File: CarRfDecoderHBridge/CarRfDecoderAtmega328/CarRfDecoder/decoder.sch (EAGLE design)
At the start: 55 parts, among them U2 RFM69CW, U3 MCP73831, U4 ATMEGA328P, U6 MIC5219 3.3V, Y1 16MHZ

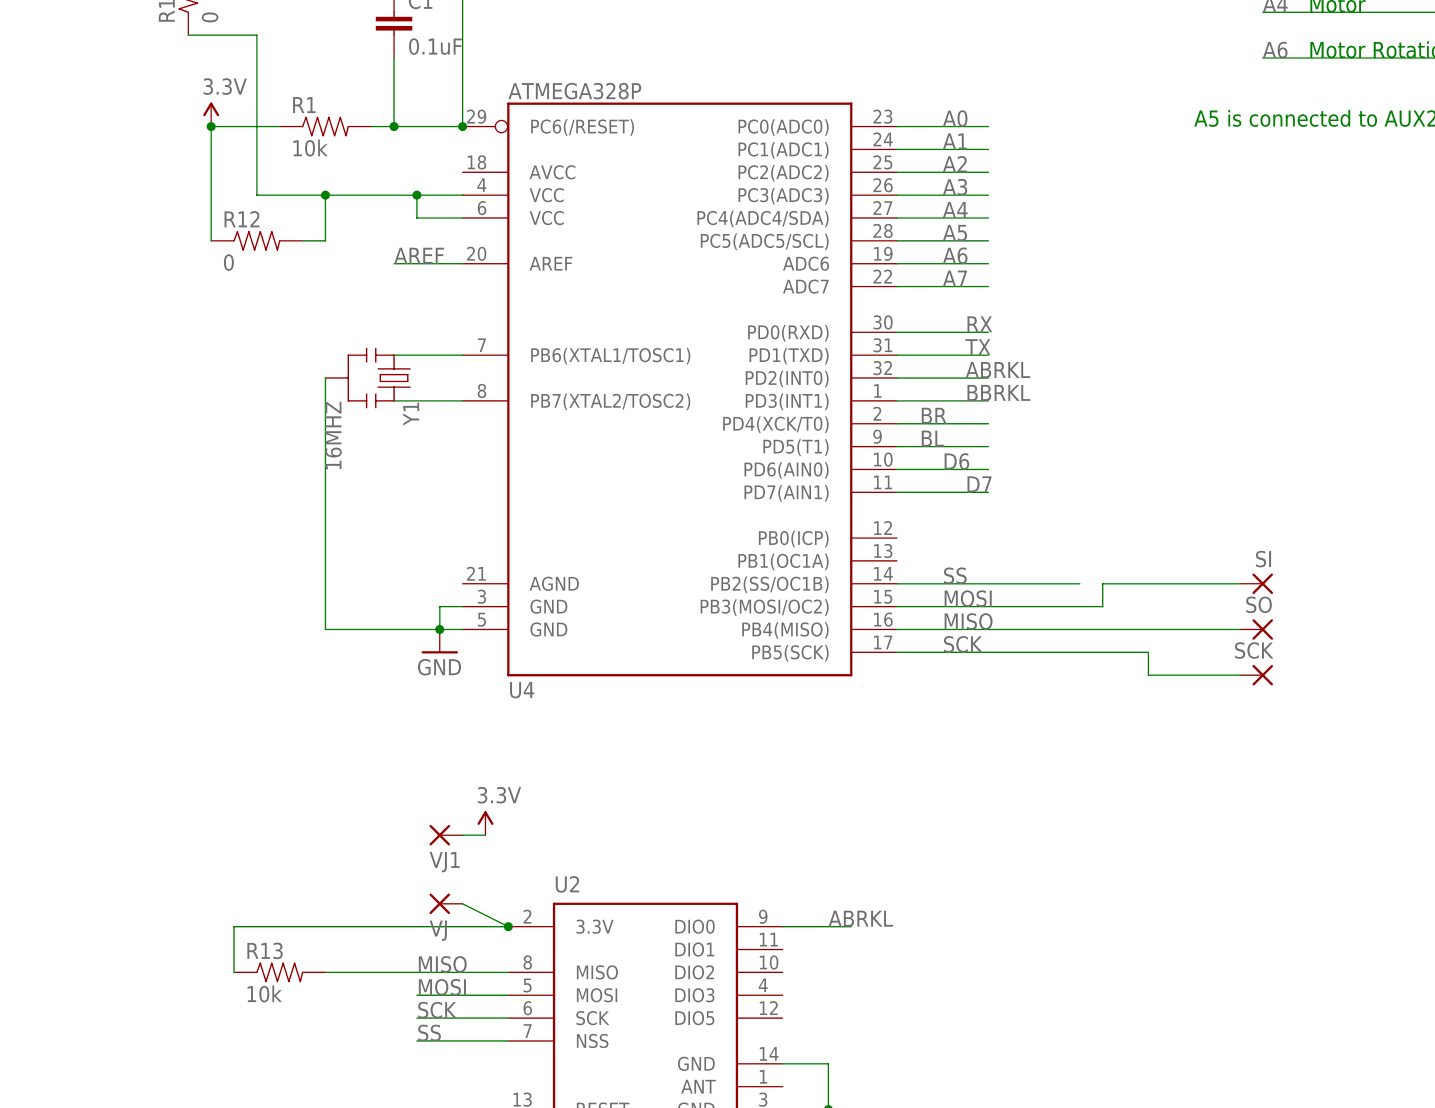
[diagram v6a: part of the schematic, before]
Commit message: Add a new version of the rc board, now smaller
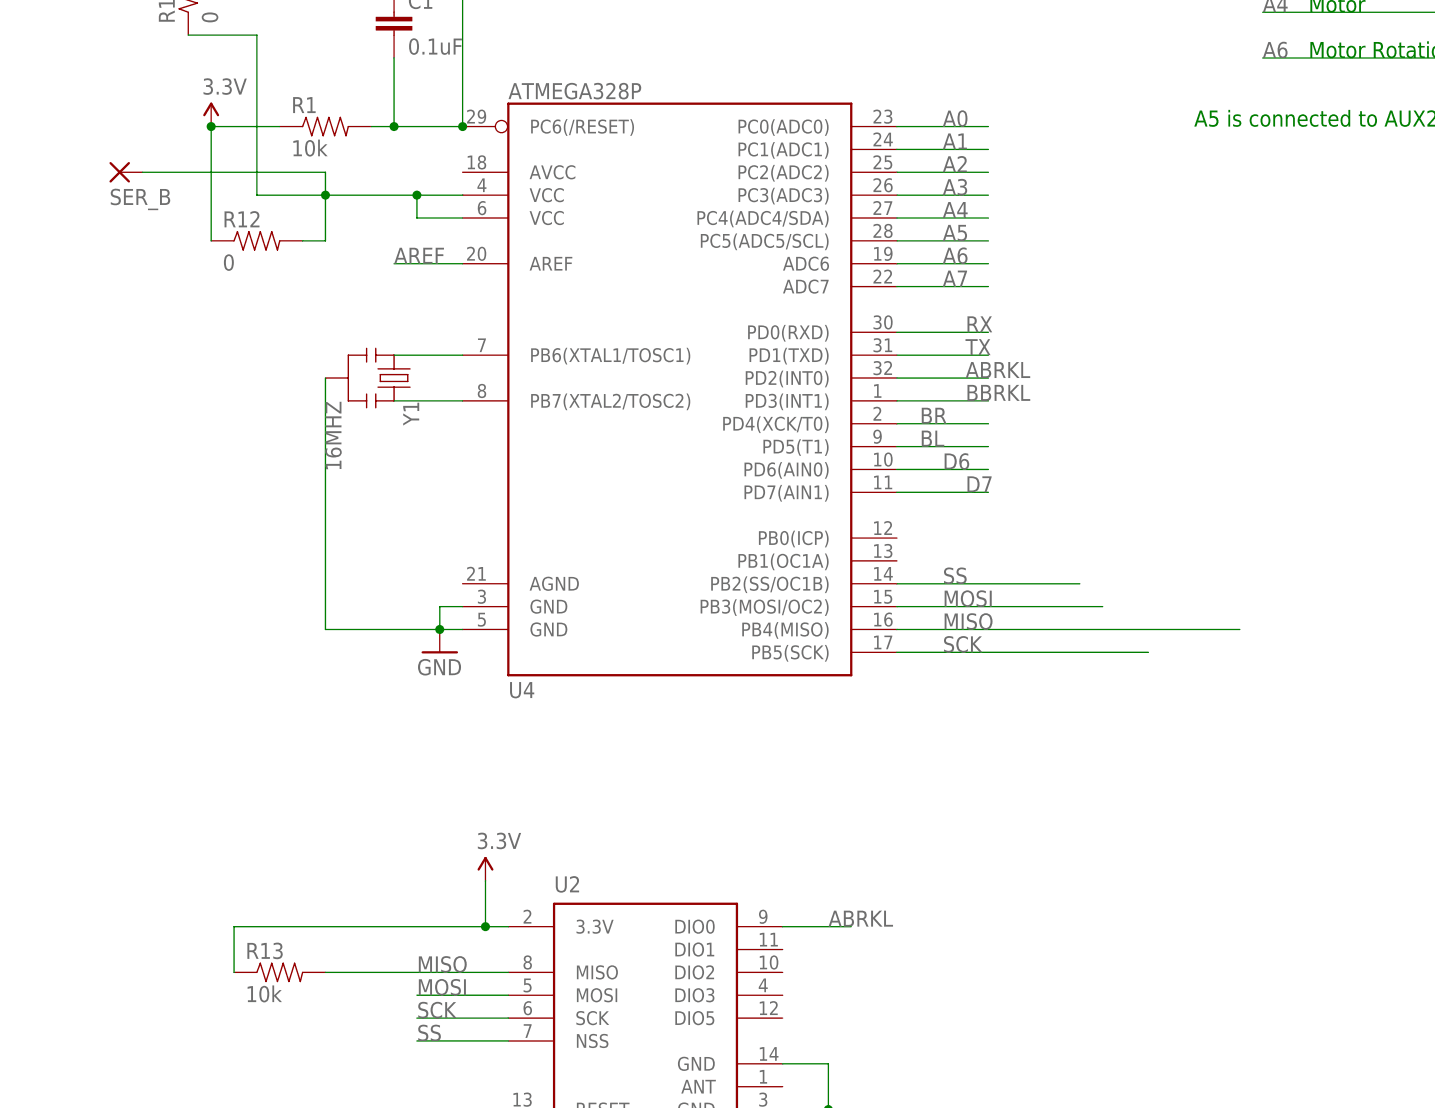
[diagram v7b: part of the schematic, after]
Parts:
- removed SCK, SI, SO, VJ, VJ1: (no value), wirepad:SMD2
- added SER_B: (no value), wirepad:SMD2
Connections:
- removed net N$1: R13.1, U2.3.3V, VJ.P
- net MISO: no longer SO.P
- net MOSI: no longer SI.P
- net N$8: now also SER_B.P
- net SCK: no longer SCK.P
- net VCC: now also R13.1, U2.3.3V; no longer VJ1.P
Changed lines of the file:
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@@
 <part name="R1" library="SparkFun-Resistors" deviceset="RESISTOR" device="0603-RES" value="10k"/>
 <part name="VCC4" library="SparkFun-Aesthetics" deviceset="VCC" device="" value="3.3V"/>
-<part name="SI" library="wirepad" deviceset="SMD2" device=""/>
-<part name="SO" library="wirepad" deviceset="SMD2" device=""/>
-<part name="SCK" library="wirepad" deviceset="SMD2" device=""/>
 <part name="SER_DTR" library="wirepad" deviceset="SMD2" device=""/>
-<part name="VJ" library="wirepad" deviceset="SMD2" device=""/>
-<part name="VJ1" library="wirepad" deviceset="SMD2" device=""/>
 <part name="Y1" library="SparkFun-FreqCtrl" deviceset="RESONATOR" device="16MHZ" value="16MHZ"/>
 <part name="GND" library="wirepad" deviceset="SMD2" device=""/>
@@
 <part name="BAT+1" library="wirepad" deviceset="SMD2" device=""/>
 <part name="R14" library="SparkFun-Resistors" deviceset="RESISTOR" device="0603-RES" value="0"/>
+<part name="SER_B" library="wirepad" deviceset="SMD2" device=""/>
 </parts>
 <sheets>
@@
 <instance part="U2" gate="G$1" x="50.8" y="-25.4"/>
 <instance part="GND12" gate="1" x="71.12" y="-40.64"/>
-<instance part="SUPPLY1" gate="G$1" x="33.02" y="-5.08"/>
+<instance part="SUPPLY1" gate="G$1" x="33.02" y="-10.16"/>
 <instance part="U4" gate="G$1" x="53.34" y="48.26"/>
 <instance part="GND3" gate="1" x="27.94" y="15.24"/>
@@
 <instance part="R1" gate="G$1" x="15.24" y="73.66"/>
 <instance part="VCC4" gate="G$1" x="2.54" y="73.66"/>
-<instance part="SI" gate="1" x="119.38" y="22.86" rot="MR0"/>
-<instance part="SO" gate="1" x="119.38" y="17.78" rot="MR0"/>
-<instance part="SCK" gate="1" x="119.38" y="12.7" rot="MR0"/>
 <instance part="SER_DTR" gate="1" x="-17.78" y="101.6"/>
-<instance part="VJ" gate="1" x="27.94" y="-12.7" rot="MR180"/>
-<instance part="VJ1" gate="1" x="27.94" y="-5.08" rot="MR180"/>
 <instance part="Y1" gate="G$1" x="22.86" y="45.72" rot="R270"/>
 <instance part="GND" gate="1" x="220.98" y="-38.1" rot="MR0"/>
@@
 <instance part="BAT+1" gate="1" x="-17.78" y="137.16"/>
 <instance part="R14" gate="G$1" x="185.42" y="91.44" rot="R180"/>
+<instance part="SER_B" gate="1" x="-7.62" y="68.58" rot="MR180"/>
 </instances>
 <busses>
@@
 </segment>
 <segment>
-<pinref part="VJ1" gate="1" pin="P"/>
-<pinref part="SUPPLY1" gate="G$1" pin="VCC"/>
-<wire x1="33.02" y1="-5.08" x2="30.48" y2="-5.08" width="0.1524" layer="91"/>
-</segment>
-<segment>
 <pinref part="R1" gate="G$1" pin="1"/>
 <wire x1="10.16" y1="73.66" x2="2.54" y2="73.66" width="0.1524" layer="91"/>
@@
 <wire x1="2.54" y1="60.96" x2="2.54" y2="73.66" width="0.1524" layer="91"/>
 <junction x="2.54" y="73.66"/>
+</segment>
+<segment>
+<pinref part="U2" gate="G$1" pin="3.3V"/>
+<pinref part="R13" gate="G$1" pin="1"/>
+<wire x1="5.08" y1="-20.32" x2="5.08" y2="-15.24" width="0.1524" layer="91"/>
+<wire x1="5.08" y1="-15.24" x2="33.02" y2="-15.24" width="0.1524" layer="91"/>
+<pinref part="SUPPLY1" gate="G$1" pin="VCC"/>
+<wire x1="33.02" y1="-15.24" x2="35.56" y2="-15.24" width="0.1524" layer="91"/>
+<wire x1="33.02" y1="-10.16" x2="33.02" y2="-15.24" width="0.1524" layer="91"/>
+<junction x="33.02" y="-15.24"/>
 </segment>
 </net>
@@
 <label x="83.82" y="15.24" size="1.778" layer="95"/>
 <wire x1="78.74" y1="15.24" x2="106.68" y2="15.24" width="0.1524" layer="91"/>
-<wire x1="106.68" y1="15.24" x2="106.68" y2="12.7" width="0.1524" layer="91"/>
-<pinref part="SCK" gate="1" pin="P"/>
-<wire x1="106.68" y1="12.7" x2="116.84" y2="12.7" width="0.1524" layer="91"/>
 </segment>
 </net>
@@
 <label x="83.82" y="20.32" size="1.778" layer="95"/>
 <wire x1="78.74" y1="20.32" x2="101.6" y2="20.32" width="0.1524" layer="91"/>
-<wire x1="101.6" y1="20.32" x2="101.6" y2="22.86" width="0.1524" layer="91"/>
-<pinref part="SI" gate="1" pin="P"/>
-<wire x1="101.6" y1="22.86" x2="116.84" y2="22.86" width="0.1524" layer="91"/>
 </segment>
 </net>
@@
 <pinref part="U4" gate="G$1" pin="PB4(MISO)"/>
 <label x="83.82" y="17.78" size="1.778" layer="95"/>
-<pinref part="SO" gate="1" pin="P"/>
 <wire x1="78.74" y1="17.78" x2="116.84" y2="17.78" width="0.1524" layer="91"/>
 </segment>
@@
 <wire x1="22.86" y1="43.18" x2="30.48" y2="43.18" width="0.1524" layer="91"/>
 <pinref part="Y1" gate="G$1" pin="3"/>
-</segment>
-</net>
-<net name="N$1" class="0">
-<segment>
-<pinref part="U2" gate="G$1" pin="3.3V"/>
-<pinref part="VJ" gate="1" pin="P"/>
-<wire x1="35.56" y1="-15.24" x2="30.48" y2="-12.7" width="0.1524" layer="91"/>
-<pinref part="R13" gate="G$1" pin="1"/>
-<wire x1="5.08" y1="-20.32" x2="5.08" y2="-15.24" width="0.1524" layer="91"/>
-<wire x1="5.08" y1="-15.24" x2="35.56" y2="-15.24" width="0.1524" layer="91"/>
-<junction x="35.56" y="-15.24"/>
 </segment>
 </net>
@@
 <pinref part="R10" gate="G$1" pin="1"/>
 <wire x1="7.62" y1="83.82" x2="0" y2="83.82" width="0.1524" layer="91"/>
-</segment>
-</net>
+<wire x1="15.24" y1="66.04" x2="15.24" y2="68.58" width="0.1524" layer="91"/>
+<pinref part="SER_B" gate="1" pin="P"/>
+<wire x1="15.24" y1="68.58" x2="-5.08" y2="68.58" width="0.1524" layer="91"/>
+</segment>
+</net>
